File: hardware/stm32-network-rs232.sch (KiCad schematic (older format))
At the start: 59 parts, among them J1 USB, M1 Mount Hole, M2 Mount Hole, M3 Mount Hole, M4 Mount Hole, P1 BELFUSE-08B0-1X1T-06-F, P2 P10, P3 DEBUG, P4 SWD, P5 RS232-TAP, P6 RS-232-DB-9-DTE, P7 P03, P8 P03, U1 ENC28J60, U2 STM32-48PIN, U3 MAX3221, U4 MOSFET-P, U5 ZLDO1117, X1 25MHz, X2 8MHz

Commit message: filters
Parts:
- added C26: 10uF, symbol CP
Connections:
- net +5V: now also C26.1
- net GNDPWR: now also C26.2
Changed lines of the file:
@@
 USBDM
 $Comp
-L +3.3V #PWR35
+L +3.3V #PWR36
 U 1 1 53B60338
 P 9800 3000
-F 0 "#PWR35" H 9800 3090 20  0001 C CNN
+F 0 "#PWR36" H 9800 3090 20  0001 C CNN
 F 1 "+3.3V" H 9800 3090 30  0000 C CNN
 F 2 "" H 9800 3000 60  0000 C CNN
@@
 $EndComp
 $Comp
-L GNDPWR #PWR36
+L GNDPWR #PWR37
 U 1 1 53B603BB
 P 9800 3600
-F 0 "#PWR36" H 9800 3650 40  0001 C CNN
+F 0 "#PWR37" H 9800 3650 40  0001 C CNN
 F 1 "GNDPWR" H 9800 3520 40  0001 C CNN
 F 2 "" H 9800 3600 60  0000 C CNN
@@
 $EndComp
 $Comp
-L GNDPWR #PWR40
+L GNDPWR #PWR41
 U 1 1 53B60B2A
 P 10500 3800
-F 0 "#PWR40" H 10500 3850 40  0001 C CNN
+F 0 "#PWR41" H 10500 3850 40  0001 C CNN
 F 1 "GNDPWR" H 10500 3720 40  0001 C CNN
 F 2 "" H 10500 3800 60  0000 C CNN
@@
 $EndComp
 $Comp
-L GNDPWR #PWR41
+L GNDPWR #PWR42
 U 1 1 53B60B43
 P 10700 3800
-F 0 "#PWR41" H 10700 3850 40  0001 C CNN
+F 0 "#PWR42" H 10700 3850 40  0001 C CNN
 F 1 "GNDPWR" H 10700 3720 40  0001 C CNN
 F 2 "" H 10700 3800 60  0000 C CNN
@@
 $EndComp
 $Comp
-L +3.3V #PWR39
+L +3.3V #PWR40
 U 1 1 53B613AF
 P 10500 2100
-F 0 "#PWR39" H 10500 2190 20  0001 C CNN
+F 0 "#PWR40" H 10500 2190 20  0001 C CNN
 F 1 "+3.3V" H 10500 2190 30  0000 C CNN
 F 2 "" H 10500 2100 60  0000 C CNN
@@
 $EndComp
 $Comp
-L +3.3V #PWR38
+L +3.3V #PWR39
 U 1 1 53B6163A
 P 10100 2100
-F 0 "#PWR38" H 10100 2190 20  0001 C CNN
+F 0 "#PWR39" H 10100 2190 20  0001 C CNN
 F 1 "+3.3V" H 10100 2190 30  0000 C CNN
 F 2 "" H 10100 2100 60  0000 C CNN
@@
 USART1TX
 $Comp
-L GNDPWR #PWR29
+L GNDPWR #PWR30
 U 1 1 53B62BA7
 P 8000 1600
-F 0 "#PWR29" H 8000 1650 40  0001 C CNN
+F 0 "#PWR30" H 8000 1650 40  0001 C CNN
 F 1 "GNDPWR" H 8000 1520 40  0001 C CNN
 F 2 "" H 8000 1600 60  0000 C CNN
@@
 $EndComp
 $Comp
-L GNDPWR #PWR31
+L GNDPWR #PWR32
 U 1 1 53B63110
 P 8000 2800
-F 0 "#PWR31" H 8000 2850 40  0001 C CNN
+F 0 "#PWR32" H 8000 2850 40  0001 C CNN
 F 1 "GNDPWR" H 8000 2720 40  0001 C CNN
 F 2 "" H 8000 2800 60  0000 C CNN
@@
 $EndComp
 $Comp
-L +3.3V #PWR30
+L +3.3V #PWR31
 U 1 1 53B63160
 P 8000 1900
-F 0 "#PWR30" H 8000 1990 20  0001 C CNN
+F 0 "#PWR31" H 8000 1990 20  0001 C CNN
 F 1 "+3.3V" H 8000 1990 30  0000 C CNN
 F 2 "" H 8000 1900 60  0000 C CNN
@@
 $EndComp
 $Comp
-L GNDPWR #PWR37
+L GNDPWR #PWR38
 U 1 1 53B6399D
 P 9900 1600
-F 0 "#PWR37" H 9900 1650 40  0001 C CNN
+F 0 "#PWR38" H 9900 1650 40  0001 C CNN
 F 1 "GNDPWR" H 9900 1520 40  0001 C CNN
 F 2 "" H 9900 1600 60  0000 C CNN
@@
 $EndComp
 $Comp
-L GNDPWR #PWR28
+L GNDPWR #PWR29
 U 1 1 53B803A1
 P 7500 5600
-F 0 "#PWR28" H 7500 5650 40  0001 C CNN
+F 0 "#PWR29" H 7500 5650 40  0001 C CNN
 F 1 "GNDPWR" H 7500 5520 40  0001 C CNN
 F 2 "" H 7500 5600 60  0000 C CNN
@@
 $EndComp
 $Comp
-L GNDPWR #PWR27
+L GNDPWR #PWR28
 U 1 1 53B806FF
 P 7200 5600
-F 0 "#PWR27" H 7200 5650 40  0001 C CNN
+F 0 "#PWR28" H 7200 5650 40  0001 C CNN
 F 1 "GNDPWR" H 7200 5520 40  0001 C CNN
 F 2 "" H 7200 5600 60  0000 C CNN
@@
 $EndComp
 $Comp
-L GNDPWR #PWR25
+L GNDPWR #PWR26
 U 1 1 53B80C7E
 P 6900 5600
-F 0 "#PWR25" H 6900 5650 40  0001 C CNN
+F 0 "#PWR26" H 6900 5650 40  0001 C CNN
 F 1 "GNDPWR" H 6900 5520 40  0001 C CNN
 F 2 "" H 6900 5600 60  0000 C CNN
@@
 $EndComp
 $Comp
-L +3.3V #PWR26
+L +3.3V #PWR27
 U 1 1 53B80DCA
 P 7200 3200
-F 0 "#PWR26" H 7200 3290 20  0001 C CNN
+F 0 "#PWR27" H 7200 3290 20  0001 C CNN
 F 1 "+3.3V" H 7200 3290 30  0000 C CNN
 F 2 "" H 7200 3200 60  0000 C CNN
@@
 $EndComp
 $Comp
-L GNDPWR #PWR34
+L GNDPWR #PWR35
 U 1 1 53B8429D
 P 9700 6300
-F 0 "#PWR34" H 9700 6350 40  0001 C CNN
+F 0 "#PWR35" H 9700 6350 40  0001 C CNN
 F 1 "GNDPWR" H 9700 6220 40  0001 C CNN
 F 2 "" H 9700 6300 60  0000 C CNN
@@
 $EndComp
 $Comp
-L GNDPWR #PWR33
+L GNDPWR #PWR34
 U 1 1 53B8524D
 P 8300 6100
-F 0 "#PWR33" H 8300 6150 40  0001 C CNN
+F 0 "#PWR34" H 8300 6150 40  0001 C CNN
 F 1 "GNDPWR" H 8300 6020 40  0001 C CNN
 F 2 "" H 8300 6100 60  0000 C CNN
@@
 $EndComp
 $Comp
-L +3.3V #PWR32
+L +3.3V #PWR33
 U 1 1 53B852CF
 P 8300 5700
-F 0 "#PWR32" H 8300 5790 20  0001 C CNN
+F 0 "#PWR33" H 8300 5790 20  0001 C CNN
 F 1 "+3.3V" H 8300 5790 30  0000 C CNN
 F 2 "" H 8300 5700 60  0000 C CNN
@@
 $EndComp
 $Comp
-L +3.3V #PWR19
+L +3.3V #PWR20
 U 1 1 53B84CAE
 P 6000 2900
-F 0 "#PWR19" H 6000 2990 20  0001 C CNN
+F 0 "#PWR20" H 6000 2990 20  0001 C CNN
 F 1 "+3.3V" H 6000 2990 30  0000 C CNN
 F 2 "" H 6000 2900 60  0000 C CNN
@@
 	6000 3000 6000 2900
 $Comp
-L GNDPWR #PWR20
+L GNDPWR #PWR21
 U 1 1 53B84DDA
 P 6000 4300
-F 0 "#PWR20" H 6000 4350 40  0001 C CNN
+F 0 "#PWR21" H 6000 4350 40  0001 C CNN
 F 1 "GNDPWR" H 6000 4220 40  0001 C CNN
 F 2 "" H 6000 4300 60  0000 C CNN
@@
 $EndComp
 $Comp
-L GNDPWR #PWR24
+L GNDPWR #PWR25
 U 1 1 53B85CCD
 P 6500 1600
-F 0 "#PWR24" H 6500 1650 40  0001 C CNN
+F 0 "#PWR25" H 6500 1650 40  0001 C CNN
 F 1 "GNDPWR" H 6500 1520 40  0001 C CNN
 F 2 "" H 6500 1600 60  0000 C CNN
@@
 $EndComp
 $Comp
-L +3.3V #PWR23
+L +3.3V #PWR24
 U 1 1 53B85DD1
 P 6500 900
-F 0 "#PWR23" H 6500 990 20  0001 C CNN
+F 0 "#PWR24" H 6500 990 20  0001 C CNN
 F 1 "+3.3V" H 6500 990 30  0000 C CNN
 F 2 "" H 6500 900 60  0000 C CNN
@@
 NoConn ~ 5800 5000
 $Comp
-L GNDPWR #PWR18
+L GNDPWR #PWR19
 U 1 1 53B9949C
 P 5400 5300
-F 0 "#PWR18" H 5400 5350 40  0001 C CNN
+F 0 "#PWR19" H 5400 5350 40  0001 C CNN
 F 1 "GNDPWR" H 5400 5220 40  0001 C CNN
 F 2 "" H 5400 5300 60  0000 C CNN
@@
 	5400 5200 5400 5300
 $Comp
-L +3.3V #PWR22
+L +3.3V #PWR23
 U 1 1 53B99624
 P 6300 4700
-F 0 "#PWR22" H 6300 4790 20  0001 C CNN
+F 0 "#PWR23" H 6300 4790 20  0001 C CNN
 F 1 "+3.3V" H 6300 4790 30  0000 C CNN
 F 2 "" H 6300 4700 60  0000 C CNN
@@
 $EndComp
 $Comp
-L GNDPWR #PWR21
+L GNDPWR #PWR22
 U 1 1 53B998C4
 P 6100 5300
-F 0 "#PWR21" H 6100 5350 40  0001 C CNN
+F 0 "#PWR22" H 6100 5350 40  0001 C CNN
 F 1 "GNDPWR" H 6100 5220 40  0001 C CNN
 F 2 "" H 6100 5300 60  0000 C CNN
@@
 Text Label 9450 4700 0    60   ~ 0
 RS232RX
+$Comp
+L CP C26
+U 1 1 53BC0E29
+P 4900 5100
+F 0 "C26" H 4925 5150 30  0000 L CNN
+F 1 "10uF" H 4925 5050 30  0000 L CNN
+F 2 "" H 4900 5100 60  0000 C CNN
+F 3 "" H 4900 5100 60  0000 C CNN
+	1    4900 5100
+	1    0    0    -1
+$EndComp
+$Comp
+L GNDPWR #PWR18
+U 1 1 53BC0EA1
+P 4900 5300
+F 0 "#PWR18" H 4900 5350 40  0001 C CNN
+F 1 "GNDPWR" H 4900 5220 40  0001 C CNN
+F 2 "" H 4900 5300 60  0000 C CNN
+F 3 "" H 4900 5300 60  0000 C CNN
+	1    4900 5300
+	1    0    0    -1
+$EndComp
+Wire Wire Line
+	4900 4900 4900 5000
+Connection ~ 4900 4900
+Wire Wire Line
+	4900 5200 4900 5300
 $EndSCHEMATC

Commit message: initial layout
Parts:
- removed C17: 0.1uF, symbol C
- L1: value 10uH -> >80mA
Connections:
- net +3.3V: no longer J1.1 (VBUS)
- net +5V: now also J1.1 (VBUS)
- net USART1RX: no longer U3.9 (ROUT)
- net USART1TX: no longer U3.11 (DIN)
- net USART2RX: now also U3.9 (ROUT)
- net USART2TX: now also U3.11 (DIN)
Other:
- note added: "ferrite bead"

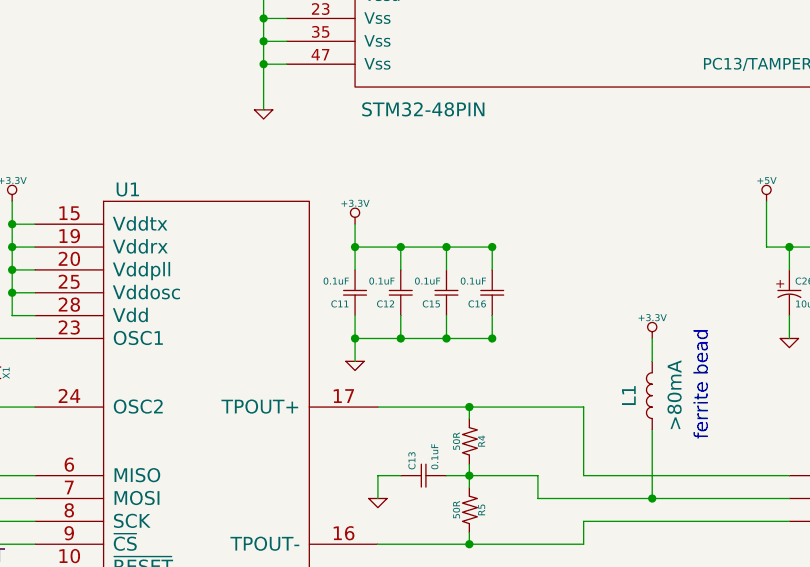
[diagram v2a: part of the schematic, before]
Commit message: upgrade to new modules part 1
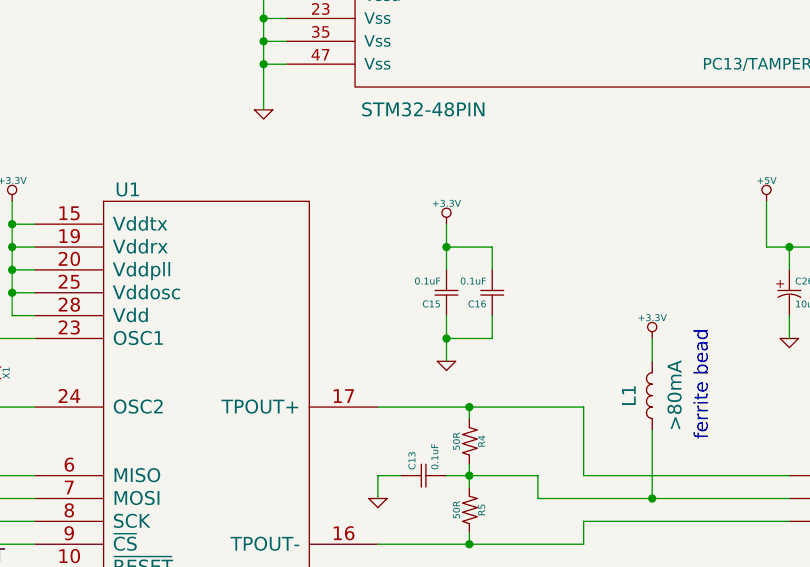
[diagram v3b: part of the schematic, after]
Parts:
- removed C11, C12: 0.1uF, symbol C
- C1, C10, C13, C14, C15, C16, C18, C19, C2, C20, C21, C22, C23, C24, C3, C4, C5, C6, C7, C8, C9: footprint (none) -> kicad-new-lib:CAPC2012X100N
- C25, C26: footprint (none) -> kicad-new-lib:CAPCP2012X100N
- D1: footprint (none) -> kicad-new-lib:LEDC3216X100N
- J1: footprint (none) -> kicad-new-lib:JST_UB-MC5BR3-SD204-4S-NMP
- L1, R1, R10, R11, R12, R2, R3, R4, R5, R6, R7, R8, R9: footprint (none) -> kicad-new-lib:RESC2012X100N
- M1, M2, M3, M4: footprint (none) -> kicad-new-lib:MTGNP565H328Z565P
- P1: footprint (none) -> kicad-new-lib:BEL-FUSE-08B0-1X1T-06-F
- P2: footprint (none) -> kicad-new-lib:HDRV10W66P254_1X10_1006X249X838P
- P3, P4, P5: footprint (none) -> kicad-new-lib:HDRV6W66P254_1X6_1524X249X838P
- P6: footprint (none) -> kicad-new-lib:TECONN-5747840-2
- P7, P8: footprint (none) -> kicad-new-lib:HDRV3W66P254_1X3_762X249X838P
- U1: footprint (none) -> kicad-new-lib:SOP65P780X200-28N
- U2: footprint (none) -> kicad-new-lib:QFP50P900X900X160-48N
- U3: footprint (none) -> kicad-new-lib:SOP65P640X120-16N
- U4: footprint (none) -> kicad-new-lib:SOT95P237X112_123-3N
- U5: footprint (none) -> kicad-new-lib:SOT230P700X180-4N
- X1, X2: footprint (none) -> kicad-new-lib:XTAL8045X200N

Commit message: add manufacturer part numbers
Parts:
- D1: MfgPartNumber (none) -> LTST-C150GKT
- J1: MfgPartNumber (none) -> UB-MC5BR3-SD204-4S-TB NMP
- L1: MfgPartNumber (none) -> HZ0805E601R-10
- P1: MfgPartNumber (none) -> 08B0-1X1T-06-F
- P6: MfgPartNumber (none) -> 5747840-2
- R1: MfgPartNumber (none) -> RNCP0805FTD2K32
- R10, R11: MfgPartNumber (none) -> RNCP0805FTD22R1
- R12: MfgPartNumber (none) -> ESR10EZPJ152
- R2, R3, R8: MfgPartNumber (none) -> RC0805JR-071KL
- R4, R5, R6, R7: MfgPartNumber (none) -> RNCP0805FTD49R9
- R9: MfgPartNumber (none) -> ESR10EZPJ103
- U1: MfgPartNumber (none) -> ENC28J60/SS
- U2: MfgPartNumber (none) -> STM32F103CBT6
- U3: MfgPartNumber (none) -> MAX3221CPWR
- U4: MfgPartNumber (none) -> ZXMP2120FFTA
- U5: MfgPartNumber (none) -> ZLDO1117G33TA
- X1: MfgPartNumber (none) -> NX8045GB-25.000000MHZ
- X2: MfgPartNumber (none) -> NX8045GB-8.000000MHZ
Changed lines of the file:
@@
 F 2 "kicad-new-lib:QFP50P900X900X160-48N" H 4050 2500 60  0001 C CNN
 F 3 "" H 4050 2500 60  0000 C CNN
+F 4 "STM32F103CBT6" H 4050 2500 60  0001 C CNN "MfgPartNumber"
 	1    4050 2500
 	1    0    0    -1
@@
 F 2 "kicad-new-lib:XTAL8045X200N" H 2500 2450 60  0001 C CNN
 F 3 "" H 2500 2450 60  0000 C CNN
+F 4 "NX8045GB-8.000000MHZ" H 2500 2450 60  0001 C CNN "MfgPartNumber"
 	1    2500 2450
 	0    1    1    0
@@
 F 2 "kicad-new-lib:JST_UB-MC5BR3-SD204-4S-NMP" H 9450 3300 60  0001 C CNN
 F 3 "" H 9450 3300 60  0000 C CNN
+F 4 "UB-MC5BR3-SD204-4S-TB NMP" H 9500 3300 60  0001 C CNN "MfgPartNumber"
 	1    9500 3300
 	1    0    0    -1
@@
 F 2 "kicad-new-lib:RESC2012X100N" H 10200 3100 60  0001 C CNN
 F 3 "" H 10200 3100 60  0000 C CNN
+F 4 "RNCP0805FTD22R1" H 10200 3100 60  0001 C CNN "MfgPartNumber"
 	1    10200 3100
 	0    1    1    0
@@
 F 2 "kicad-new-lib:RESC2012X100N" H 10200 3400 60  0001 C CNN
 F 3 "" H 10200 3400 60  0000 C CNN
+F 4 "RNCP0805FTD22R1" H 10200 3400 60  0001 C CNN "MfgPartNumber"
 	1    10200 3400
 	0    1    1    0
@@
 F 2 "kicad-new-lib:RESC2012X100N" H 10500 2900 60  0001 C CNN
 F 3 "" H 10500 2900 60  0000 C CNN
+F 4 "ESR10EZPJ152" H 10500 2900 60  0001 C CNN "MfgPartNumber"
 	1    10500 2900
 	-1   0    0    1
@@
 F 2 "kicad-new-lib:SOT95P237X112_123-3N" H 10500 2450 60  0001 C CNN
 F 3 "" H 10500 2450 60  0000 C CNN
+F 4 "ZXMP2120FFTA" H 10500 2500 60  0001 C CNN "MfgPartNumber"
 	1    10500 2500
 	1    0    0    -1
@@
 F 2 "kicad-new-lib:RESC2012X100N" H 10100 2300 60  0001 C CNN
 F 3 "" H 10100 2300 60  0000 C CNN
+F 4 "ESR10EZPJ103" H 10100 2300 60  0001 C CNN "MfgPartNumber"
 	1    10100 2300
 	-1   0    0    1
@@
 F 2 "kicad-new-lib:SOP65P640X120-16N" H 8200 4000 60  0001 C CNN
 F 3 "" H 8200 4000 60  0000 C CNN
+F 4 "MAX3221CPWR" H 8400 4300 60  0001 C CNN "MfgPartNumber"
 	1    8400 4300
 	1    0    0    -1
@@
 F 2 "kicad-new-lib:TECONN-5747840-2" H 10100 5000 60  0001 C CNN
 F 3 "" H 10100 5000 60  0000 C CNN
+F 4 "5747840-2" H 10300 5600 60  0001 C CNN "MfgPartNumber"
 	1    10300 5600
 	1    0    0    -1
@@
 F 2 "kicad-new-lib:XTAL8045X200N" H 1400 5450 60  0001 C CNN
 F 3 "" H 1400 5450 60  0000 C CNN
+F 4 "NX8045GB-25.000000MHZ" H 1400 5450 60  0001 C CNN "MfgPartNumber"
 	1    1400 5450
 	0    1    1    0
@@
 F 2 "kicad-new-lib:RESC2012X100N" H 950 7200 60  0001 C CNN
 F 3 "" H 950 7200 60  0000 C CNN
+F 4 "RNCP0805FTD2K32" H 950 7200 60  0001 C CNN "MfgPartNumber"
 	1    950  7200
 	-1   0    0    1
@@
 F 2 "kicad-new-lib:LEDC3216X100N" H 6500 1100 60  0001 C CNN
 F 3 "" H 6500 1100 60  0000 C CNN
+F 4 "LTST-C150GKT" H 6500 1100 60  0001 C CNN "MfgPartNumber"
 	1    6500 1100
 	0    1    1    0
@@
 F 2 "kicad-new-lib:RESC2012X100N" H 6500 1400 60  0001 C CNN
 F 3 "" H 6500 1400 60  0000 C CNN
+F 4 "RC0805JR-071KL" H 6500 1400 60  0001 C CNN "MfgPartNumber"
 	1    6500 1400
 	-1   0    0    1
@@
 F 2 "kicad-new-lib:BEL-FUSE-08B0-1X1T-06-F" H 5200 6000 60  0001 C CNN
 F 3 "" H 5200 6000 60  0000 C CNN
+F 4 "08B0-1X1T-06-F" H 5600 6400 60  0001 C CNN "MfgPartNumber"
 	1    5600 6400
 	1    0    0    -1
@@
 F 2 "kicad-new-lib:RESC2012X100N" H 3500 5750 60  0001 C CNN
 F 3 "" H 3500 5750 60  0000 C CNN
+F 4 "RNCP0805FTD49R9" H 3500 5750 60  0001 C CNN "MfgPartNumber"
 	1    3500 5750
 	-1   0    0    1
@@
 F 2 "kicad-new-lib:RESC2012X100N" H 3500 6050 60  0001 C CNN
 F 3 "" H 3500 6050 60  0000 C CNN
+F 4 "RNCP0805FTD49R9" H 3500 6050 60  0001 C CNN "MfgPartNumber"
 	1    3500 6050
 	-1   0    0    1
@@
 F 2 "kicad-new-lib:RESC2012X100N" H 3300 7200 60  0001 C CNN
 F 3 "" H 3300 7200 60  0000 C CNN
+F 4 "RC0805JR-071KL" H 3300 7200 60  0001 C CNN "MfgPartNumber"
 	1    3300 7200
 	0    -1   -1   0
@@
 F 2 "kicad-new-lib:RESC2012X100N" H 3300 7400 60  0001 C CNN
 F 3 "" H 3300 7400 60  0000 C CNN
+F 4 "RC0805JR-071KL" H 3300 7400 60  0001 C CNN "MfgPartNumber"
 	1    3300 7400
 	0    -1   -1   0
@@
 F 2 "kicad-new-lib:RESC2012X100N" H 3500 6550 60  0001 C CNN
 F 3 "" H 3500 6550 60  0000 C CNN
+F 4 "RNCP0805FTD49R9" H 3500 6550 60  0001 C CNN "MfgPartNumber"
 	1    3500 6550
 	-1   0    0    1
@@
 F 2 "kicad-new-lib:RESC2012X100N" H 3500 6850 60  0001 C CNN
 F 3 "" H 3500 6850 60  0000 C CNN
+F 4 "RNCP0805FTD49R9" H 3500 6850 60  0001 C CNN "MfgPartNumber"
 	1    3500 6850
 	-1   0    0    1
@@
 F 2 "kicad-new-lib:RESC2012X100N" H 4300 5550 60  0001 C CNN
 F 3 "" H 4300 5550 60  0000 C CNN
+F 4 "HZ0805E601R-10" H 4300 5550 60  0001 C CNN "MfgPartNumber"
 	1    4300 5550
 	0    1    1    0
@@
 F 2 "kicad-new-lib:SOT230P700X180-4N" H 5400 4950 60  0001 C CNN
 F 3 "" H 5400 4950 60  0000 C CNN
+F 4 "ZLDO1117G33TA" H 5400 4950 60  0001 C CNN "MfgPartNumber"
 	1    5400 4950
 	1    0    0    -1
@@
 F 2 "kicad-new-lib:SOP65P780X200-28N" H 3000 5650 60  0001 C CNN
 F 3 "" H 3000 5650 60  0000 C CNN
+F 4 "ENC28J60/SS" H 2300 6200 60  0001 C CNN "MfgPartNumber"
 	1    2300 6200
 	1    0    0    -1
